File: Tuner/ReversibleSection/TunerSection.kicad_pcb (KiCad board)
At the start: 2 copper layers, 100 x 100 mm, 97 parts, among them J1 Conn_01x03, J10 Conn_01x02, J11 Conn_01x05, J12 Conn_01x01, J13 Conn_01x01, J14 Conn_01x01, J15 Conn_01x01, J2 Conn_01x03, J3 Conn_01x03, J4 Conn_01x03, J5 Conn_01x03, J6 Conn_01x03, J7 Conn_01x03, J8 Conn_01x02, J9 Conn_01x02, P10 Conn_01x01, P11 Conn_01x01, P12 Conn_01x01, P2 Conn_01x01, P3 Conn_01x01, P4 Conn_01x01, P5 Conn_01x01, P6 Conn_01x01, P7 Conn_01x01, P8 Conn_01x01, P9 Conn_01x01, U1 MCP23008, U2 ULN2803A

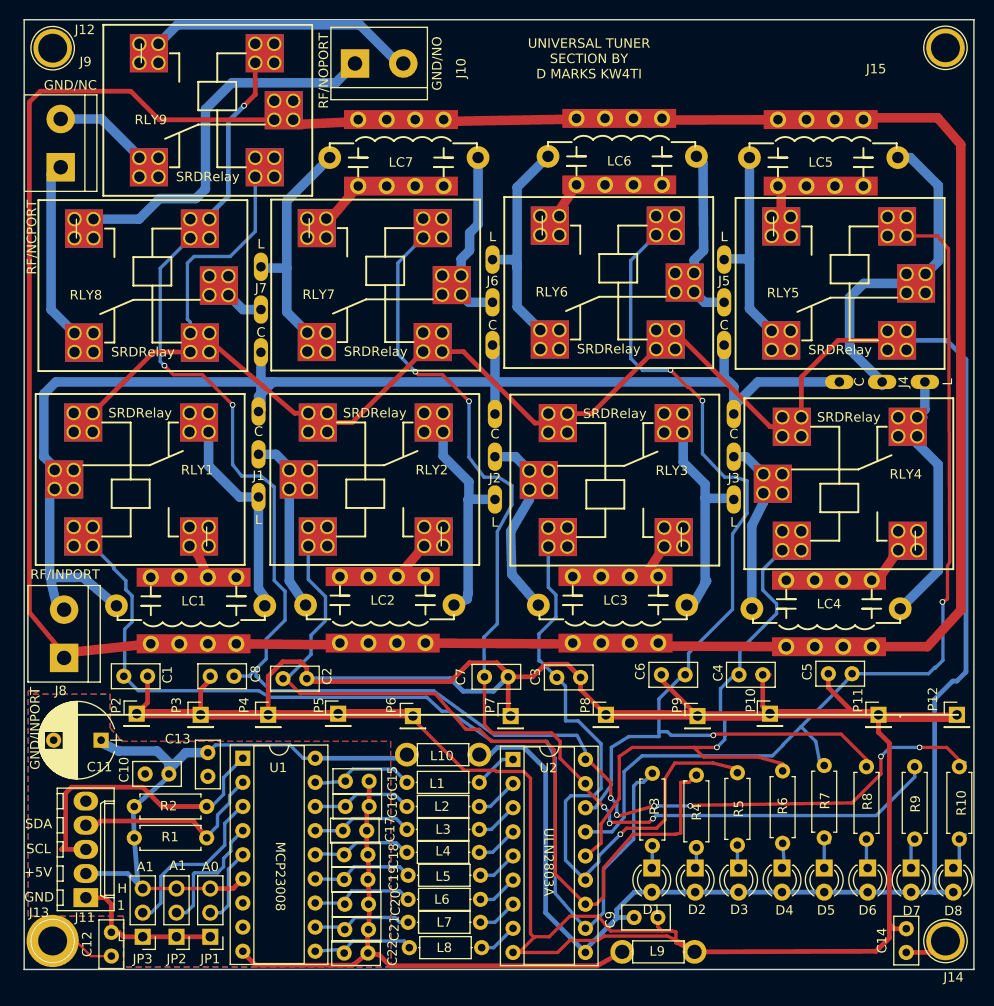
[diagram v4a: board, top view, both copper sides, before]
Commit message: JLCPCB submitted RelayControl version
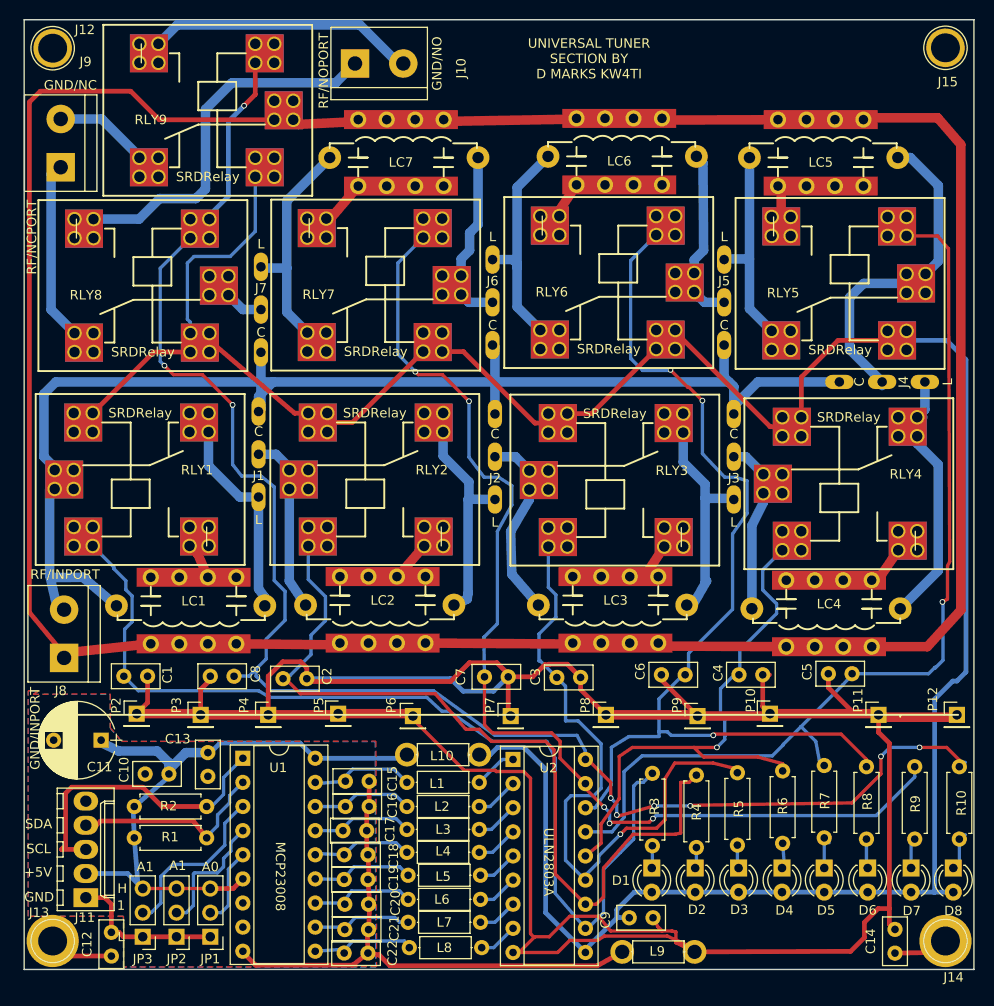
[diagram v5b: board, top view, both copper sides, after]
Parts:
- moved C14 1.19 mm to (141.7, 148.3)
- moved C9 0.51 mm to (113.7, 144.6)
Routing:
- net Net-(C14-Pad1): track 4.63 -> 5.82 mm
- net RLYPWR: track 264.9 -> 264.4 mm
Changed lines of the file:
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@@
     (thickness 1.6)
     (drawings 26)
-    (tracks 810)
+    (tracks 812)
     (zones 0)
     (modules 97)
@@
     (fp_circle (center 0 0) (end 2.6 0) (layer F.CrtYd) (width 0.05))
     (fp_circle (center 0 0) (end 0 -2.286) (layer F.SilkS) (width 0.12))
-    (pad 1 thru_hole circle (at 0 0) (size 4.064 4.064) (drill 3.048) (layers *.Cu *.Mask)
+    (pad 1 thru_hole circle (at 0 0) (size 5.5 5.5) (drill 3.048) (layers *.Cu *.Mask)
       (net 70 "Net-(C14-Pad1)"))
   )
@@
     (descr "module 1 pin (ou trou mecanique de percage)")
     (tags DEV)
-    (fp_text reference J15 (at -7.3 2.225) (layer F.SilkS)
+    (fp_text reference J15 (at 0.2413 3.59156) (layer F.SilkS)
       (effects (font (size 1 1) (thickness 0.15)))
     )
@@
     (descr "LED, diameter 3.0mm, 2 pins")
     (tags "LED diameter 3.0mm 2 pins")
-    (fp_text reference D1 (at 4.3815 0 360) (layer F.SilkS)
+    (fp_text reference D1 (at 1.31572 3.24104 360) (layer F.SilkS)
       (effects (font (size 1 1) (thickness 0.15)))
     )
@@
   )
   (module Capacitors_THT:C_Disc_D5.0mm_W2.5mm_P2.50mm (layer F.Cu)
-    (at 114.2238 144.526)
+    (at 113.71072 144.55648)
     (descr "C, Disc series, Radial, pin pitch=2.50mm, , diameter*width=5*2.5mm^2, Capacitor, http://cdn-reichelt.de/documents/datenblatt/B300/DS_KERKO_TC.pdf")
     (tags "C Disc series Radial pin pitch 2.50mm  diameter 5mm width 2.5mm Capacitor")
@@
   )
   (module Capacitors_THT:C_Disc_D5.0mm_W2.5mm_P2.50mm (layer F.Cu)
-    (at 142.875 148.209 90)
+    (at 141.68628 148.28012 90)
     (descr "C, Disc series, Radial, pin pitch=2.50mm, , diameter*width=5*2.5mm^2, Capacitor, http://cdn-reichelt.de/documents/datenblatt/B300/DS_KERKO_TC.pdf")
     (tags "C Disc series Radial pin pitch 2.50mm  diameter 5mm width 2.5mm Capacitor")
@@
   (segment (start 74.3326 57.8744) (end 74.3326 54.53836) (width 0.5) (layer F.Cu) (net 33) (status 20))
   (segment (start 67.5 72.994) (end 67.214 72.994) (width 0.35) (layer F.Cu) (net 33) (status 30))
+  (segment (start 69.342 127.167) (end 69.61696 127.167) (width 0.5) (layer B.Cu) (net 34) (status C00000))
+  (segment (start 69.61696 127.167) (end 70.63232 126.15164) (width 0.5) (layer B.Cu) (net 34) (status 400000))
+  (segment (start 79.03464 126.15164) (end 80.645 127.762) (width 0.5) (layer B.Cu) (net 34) (status 800000))
+  (segment (start 70.63232 126.15164) (end 79.03464 126.15164) (width 0.5) (layer B.Cu) (net 34))
   (segment (start 69.596 141.478) (end 72.009 141.478) (width 0.5) (layer F.Cu) (net 34))
   (segment (start 72.009 141.478) (end 73.025 140.462) (width 0.5) (layer F.Cu) (net 34))
@@
   (segment (start 80.645 127.762) (end 89.916 127.762) (width 0.5) (layer B.Cu) (net 34) (status 30))
   (segment (start 89.916 127.762) (end 90.297 127.381) (width 0.5) (layer B.Cu) (net 34) (status 30))
-  (segment (start 80.645 127.762) (end 79.375 127.762) (width 0.35) (layer B.Cu) (net 34) (status 10))
-  (segment (start 70.144 126.365) (end 69.342 127.167) (width 0.35) (layer B.Cu) (net 34) (status 20))
-  (segment (start 77.978 126.365) (end 70.144 126.365) (width 0.35) (layer B.Cu) (net 34))
-  (segment (start 79.375 127.762) (end 77.978 126.365) (width 0.35) (layer B.Cu) (net 34))
   (segment (start 61.722 136.017) (end 61.595 136.144) (width 0.35) (layer B.Cu) (net 34) (status 30))
   (segment (start 65.238 129.413) (end 65.238 128.945) (width 1) (layer B.Cu) (net 34) (status 30))
@@
   (segment (start 148.463 138.684) (end 147.828 139.319) (width 0.35) (layer B.Cu) (net 50))
   (segment (start 148.9456 135.9662) (end 149.098 135.8138) (width 0.35) (layer B.Cu) (net 50) (status 30))
-  (segment (start 142.875 145.709) (end 141.5815 145.709) (width 0.5) (layer F.Cu) (net 51))
+  (segment (start 141.097 143.5862) (end 139.92352 143.5862) (width 0.5) (layer F.Cu) (net 51))
+  (segment (start 138.47064 146.6342) (end 137.013916 148.090924) (width 0.5) (layer F.Cu) (net 51))
+  (segment (start 138.47064 145.03908) (end 138.47064 146.6342) (width 0.5) (layer F.Cu) (net 51))
+  (segment (start 139.92352 143.5862) (end 138.47064 145.03908) (width 0.5) (layer F.Cu) (net 51))
+  (segment (start 141.68628 145.78012) (end 141.5815 145.709) (width 0.5) (layer F.Cu) (net 51) (status 10))
   (segment (start 141.5815 145.709) (end 141.097 145.2245) (width 0.5) (layer F.Cu) (net 51))
-  (segment (start 116.7238 144.526) (end 116.7238 145.502) (width 0.35) (layer F.Cu) (net 51))
+  (segment (start 116.21072 144.55648) (end 116.7238 145.502) (width 0.35) (layer F.Cu) (net 51) (status 10))
   (segment (start 116.7238 145.502) (end 117.1702 145.9484) (width 0.35) (layer F.Cu) (net 51))
   (segment (start 90.932 123.317) (end 90.932 123.6345) (width 0.35) (layer F.Cu) (net 51))
@@
   (segment (start 99.568 129.032) (end 99.695 129.159) (width 0.35) (layer F.Cu) (net 51))
   (segment (start 96.3295 129.032) (end 99.568 129.032) (width 0.35) (layer F.Cu) (net 51))
-  (segment (start 120.5865 148.1455) (end 139.7 148.082) (width 0.5) (layer F.Cu) (net 51) (status 10))
+  (segment (start 120.5865 148.1455) (end 137.013916 148.090924) (width 0.5) (layer F.Cu) (net 51) (status 10))
   (segment (start 139.954 125.0315) (end 139.954 123.19) (width 0.5) (layer F.Cu) (net 51))
   (segment (start 141.097 126.1745) (end 139.954 125.0315) (width 0.5) (layer F.Cu) (net 51))
-  (segment (start 141.097 146.685) (end 141.097 145.2245) (width 0.5) (layer F.Cu) (net 51))
-  (segment (start 141.097 145.2245) (end 141.097 126.1745) (width 0.5) (layer F.Cu) (net 51))
-  (segment (start 139.7 148.082) (end 141.097 146.685) (width 0.5) (layer F.Cu) (net 51))
+  (segment (start 141.097 145.2245) (end 141.097 143.5862) (width 0.5) (layer F.Cu) (net 51))
+  (segment (start 141.097 143.5862) (end 141.097 126.1745) (width 0.5) (layer F.Cu) (net 51))
   (segment (start 62.992 119.126) (end 62.992 121.92) (width 0.5) (layer F.Cu) (net 51))
   (segment (start 62.992 121.92) (end 61.849 123.063) (width 0.5) (layer F.Cu) (net 51))
@@
   (segment (start 127.762 118.9736) (end 128.4732 118.9736) (width 0.5) (layer F.Cu) (net 51) (status 30))
   (segment (start 62.992 119.126) (end 62.992 119.3165) (width 0.5) (layer F.Cu) (net 51) (status 30))
-  (segment (start 114.2238 144.526) (end 112.4585 144.526) (width 0.5) (layer B.Cu) (net 52))
+  (segment (start 113.71072 144.55648) (end 112.4585 144.526) (width 0.5) (layer B.Cu) (net 52) (status 10))
   (segment (start 112.4585 144.526) (end 112.395 144.5895) (width 0.5) (layer B.Cu) (net 52))
   (segment (start 145.8595 141.859) (end 145.8595 121.539) (width 0.5) (layer B.Cu) (net 52))
@@
   (segment (start 98.171 147.701) (end 99.441 147.701) (width 0.35) (layer B.Cu) (net 68) (status 10))
   (segment (start 99.441 147.701) (end 101.473 145.669) (width 0.35) (layer B.Cu) (net 68) (status 20))
-  (segment (start 59.182 148.59) (end 57.023 148.59) (width 0.25) (layer F.Cu) (net 69))
-  (segment (start 55.433 147) (end 53 147) (width 0.25) (layer F.Cu) (net 69))
-  (segment (start 57.023 148.59) (end 55.433 147) (width 0.25) (layer F.Cu) (net 69))
-  (segment (start 142.875 148.209) (end 145.796 148.209) (width 0.5) (layer F.Cu) (net 70))
+  (segment (start 59.182 148.59) (end 54.59 148.59) (width 0.5) (layer F.Cu) (net 69))
+  (segment (start 54.59 148.59) (end 53 147) (width 0.5) (layer F.Cu) (net 69))
+  (segment (start 141.68628 148.28012) (end 145.796 148.209) (width 0.5) (layer F.Cu) (net 70) (status 10))
   (segment (start 145.796 148.209) (end 147.0025 147.0025) (width 0.5) (layer F.Cu) (net 70))
   (zone (net 25) (net_name GND) (layer F.Cu) (hatch edge 0.508)
@@
     (polygon
       (pts
-        (xy 50.927 121.031) (xy 59.055 120.9675) (xy 59.055 124.5235) (xy 60.2615 125.984) (xy 88.5825 125.984)
-        (xy 88.646 149.733) (xy 60.452 149.733) (xy 60.452 144.399) (xy 50.419 144.399) (xy 50.419 120.65)
+        (xy 50.927 121.031) (xy 59.055 120.9675) (xy 59.055 124.5235) (xy 60.2615 125.984) (xy 87.04326 125.9586)
+        (xy 87.10676 149.7076) (xy 60.452 149.733) (xy 60.452 144.399) (xy 50.419 144.399) (xy 50.419 120.65)
         (xy 50.673 120.65) (xy 51.562 120.65)
       )
@@
     (polygon
       (pts
-        (xy 50.927 121.031) (xy 59.055 121.031) (xy 59.055 124.587) (xy 60.2615 125.984) (xy 88.5825 125.984)
-        (xy 88.646 149.733) (xy 60.452 149.733) (xy 60.452 144.399) (xy 50.419 144.399) (xy 50.419 120.65)
+        (xy 50.927 121.031) (xy 59.055 121.031) (xy 59.055 124.587) (xy 60.2615 125.984) (xy 86.96198 126.0094)
+        (xy 87.02548 149.7584) (xy 60.452 149.733) (xy 60.452 144.399) (xy 50.419 144.399) (xy 50.419 120.65)
         (xy 50.673 120.65) (xy 51.562 120.65)
       )

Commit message: JLCPCB order 09232018 - improved grounding - improved I2C cabling - NEO7M port - support for common mode chokes - relay board now has capacitors on all coils
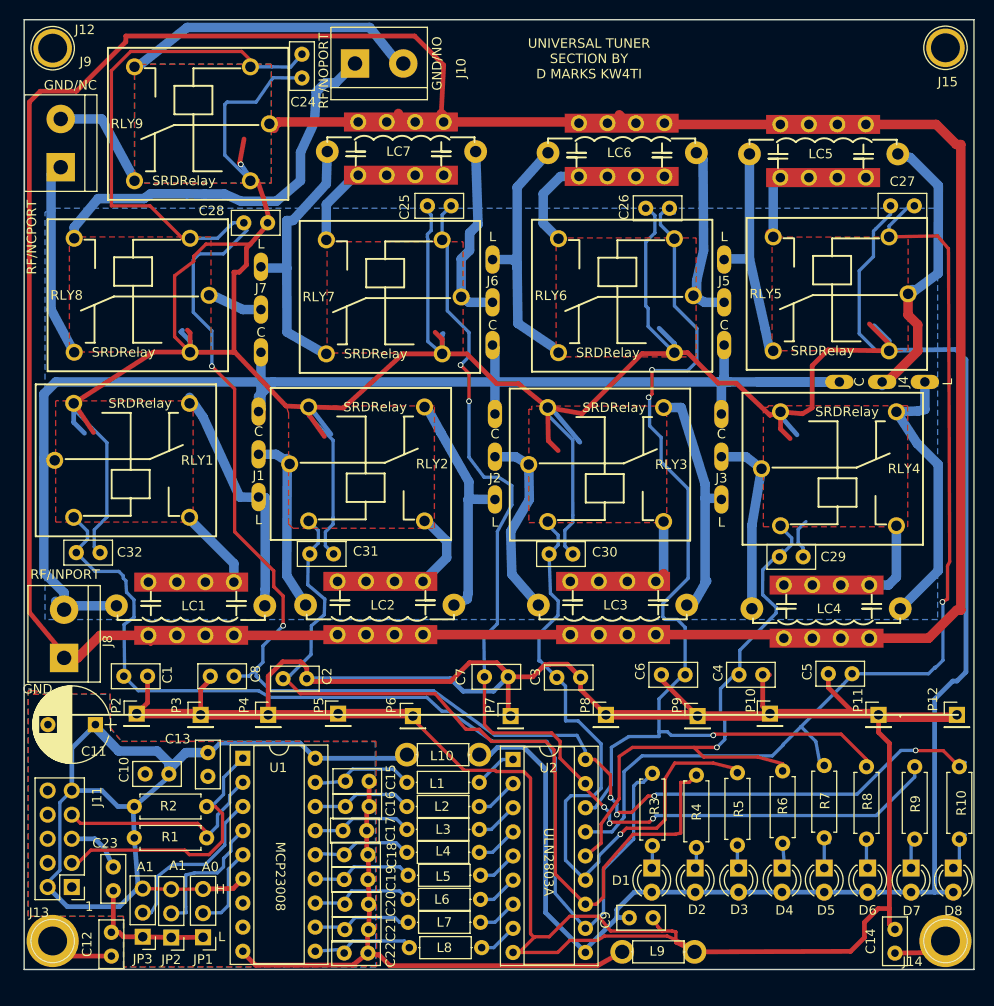
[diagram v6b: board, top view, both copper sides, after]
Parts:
- added C23: 100 nF, Capacitors_THT:C_Disc_D5.0mm_W2.5mm_P2.50mm, F.Cu at (59.4, 141.7)
- added C24: 10 nF, Capacitors_THT:C_Disc_D5.0mm_W2.5mm_P2.50mm, F.Cu at (79.2, 56.1)
- added C25: 10 nF, Capacitors_THT:C_Disc_D5.0mm_W2.5mm_P2.50mm, F.Cu at (92.5, 69.6)
- added C26: 10 nF, Capacitors_THT:C_Disc_D5.0mm_W2.5mm_P2.50mm, F.Cu at (115.4, 69.8)
- added C27: 10 nF, Capacitors_THT:C_Disc_D5.0mm_W2.5mm_P2.50mm, F.Cu at (141.2, 69.6)
- added C28: 10 nF, Capacitors_THT:C_Disc_D5.0mm_W2.5mm_P2.50mm, F.Cu at (75.6, 71.4)
- added C29: 10 nF, Capacitors_THT:C_Disc_D5.0mm_W2.5mm_P2.50mm, F.Cu at (132.0, 106.6)
- added C30: 10 nF, Capacitors_THT:C_Disc_D5.0mm_W2.5mm_P2.50mm, F.Cu at (107.8, 106.3)
- added C31: 10 nF, Capacitors_THT:C_Disc_D5.0mm_W2.5mm_P2.50mm, F.Cu at (82.6, 106.2)
- added C32: 10 nF, Capacitors_THT:C_Disc_D5.0mm_W2.5mm_P2.50mm, F.Cu at (58.0, 106.1)
- J11: value Conn_01x05 -> Conn_02x05_Odd_Even; footprint Connectors_Molex:Molex_KK-6410-05_05x2.54mm_Straight -> Pin_Headers:Pin_Header_Straight_2x05_Pitch2.54mm
- moved RLY9 2.55 mm to (67.8, 61.0)
- moved RLY8 2.03 mm to (61.5, 79.0)
- moved J11 1.86 mm to (55.0, 141.3), turned to 180 degrees
- moved RLY5 1.84 mm to (135.1, 78.9)
- moved C11 1.74 mm to (57.5, 124.2)
- moved J3 1.31 mm to (123.4, 96.0)
- moved RLY1 1.02 mm to (61.2, 96.4)
- moved JP1 0.76 mm to (68.8, 146.6)
- moved LC7 0.68 mm to (89.9, 63.9)
- moved RLY3 0.64 mm to (111.1, 96.8)
- moved RLY2 0.64 mm to (86.0, 96.8)
- moved RLY4 0.60 mm to (135.6, 97.3)
- moved JP2 0.56 mm to (65.5, 146.6)
- moved RLY6 0.39 mm to (112.5, 79.1)
- moved LC5 0.38 mm to (134.4, 64.1)
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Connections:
- net Net-(J11-Pad3) renamed SCL
- J11 pad 4: Net-(J11-Pad4) -> GND
- J11 pad 5: (no net) -> Net-(C23-Pad2)
- R1 pad 2: Net-(J11-Pad4) -> SDA
- U1 pad 2: Net-(J11-Pad4) -> SDA
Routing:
- net RLYPWR: track 264.4 -> 468.2 mm, vias 0 -> 1
- net RLY8: track 166.0 -> 200.9 mm, vias 9 -> 6
- net +5V: track 69.3 -> 102.3 mm
- net SDA: track 0.00 -> 23.0 mm
- net Net-(J11-Pad4): track 21.2 -> 0.00 mm
- net RFGND: track 264.9 -> 281.2 mm
- net RFPORT1: track 144.4 -> 153.6 mm
- net RLY1: track 103.5 -> 110.8 mm
- net RLY5: track 101.9 -> 108.4 mm
- net Net-(LC6-Pad1): track 3.84 -> 9.92 mm
- net Net-(C23-Pad2): track 0.00 -> 6.03 mm
- net Net-(LC1-Pad1): track 3.88 -> 8.76 mm
- net Net-(J7-Pad1): track 24.2 -> 29.1 mm
- net Net-(J4-Pad1): track 25.4 -> 29.9 mm
- net RLY4: track 58.4 -> 62.8 mm
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- added copper zone on B.Cu, net RLYPWR
- added copper zone on F.Cu, net RLYPWR
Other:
- board text removed: "+5V"
- board text removed: "GND/INPORT"
- board text removed: "SCL"
- board text removed: "SDA"

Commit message: Relay boards changed to have coil terminals all on same side
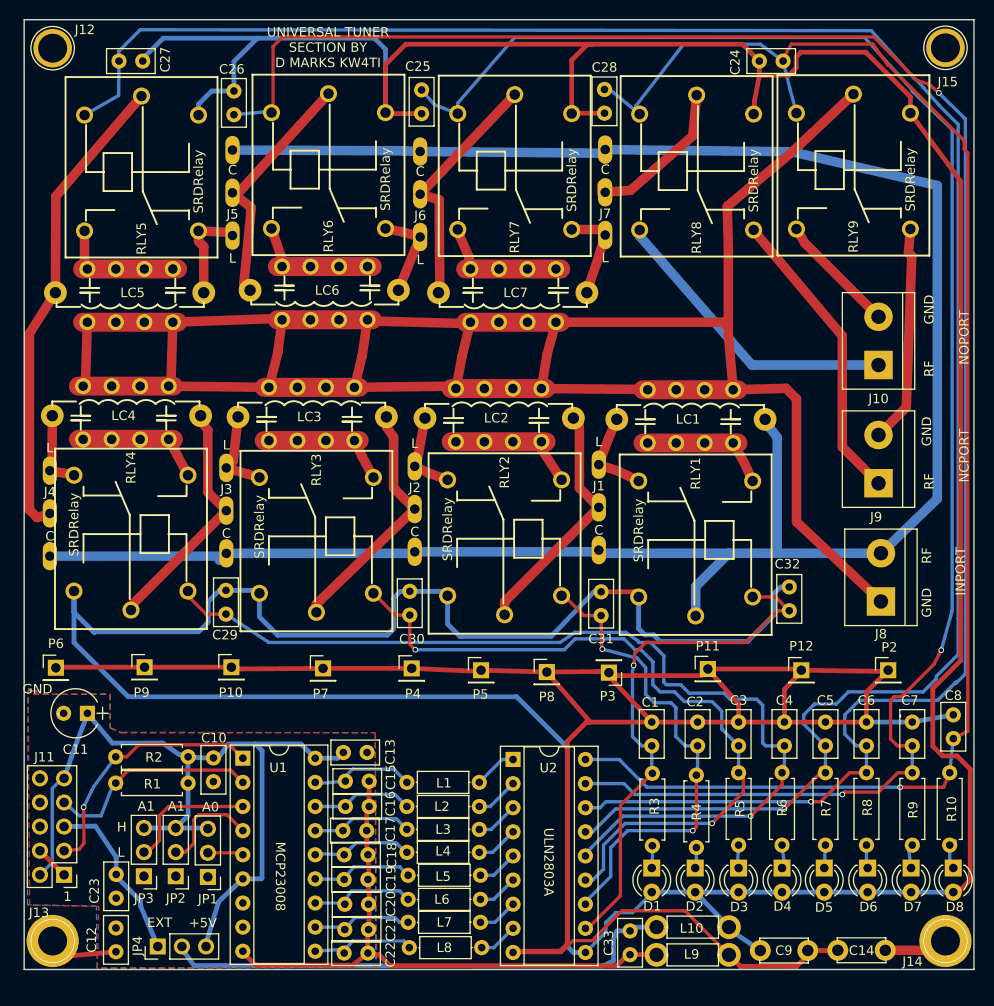
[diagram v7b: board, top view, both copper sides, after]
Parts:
- added C33: 100 nF, Capacitors_THT:C_Disc_D5.0mm_W2.5mm_P2.50mm, F.Cu at (113.8, 148.4)
- added JP4: Jumper_NC_Dual, Pin_Headers:Pin_Header_Straight_1x03_Pitch2.54mm, F.Cu at (64.1, 147.6)
- C11: footprint Capacitors_THT:CP_Radial_D8.0mm_P5.00mm -> Capacitors_THT:CP_Radial_Tantal_D5.0mm_P2.50mm
- C14, C9: footprint Capacitors_THT:C_Disc_D5.0mm_W2.5mm_P2.50mm -> Capacitors_THT:C_Disc_D5.0mm_W2.5mm_P5.00mm
- moved J9 92.3 mm to (140.0, 98.8)
- moved J4 88.7 mm to (52.7, 102.0), turned to 270 degrees
- moved J8 86.2 mm to (140.2, 111.3)
- moved C27 80.2 mm to (62.5, 54.4), turned to 180 degrees
- moved P2 79.3 mm to (141.0, 118.5)
- moved C8 78.3 mm to (147.8, 123.2), turned to 270 degrees
- moved LC4 76.0 mm to (61.0, 91.7), turned to 90 degrees
- moved LC5 74.9 mm to (60.9, 78.7), turned to 270 degrees
- moved RLY4 74.7 mm to (61.2, 104.2), turned to 90 degrees
- moved RLY5 73.8 mm to (62.4, 66.0), turned to 270 degrees
- moved C32 72.7 mm to (130.6, 109.7), turned to 270 degrees
- moved RLY9 69.7 mm to (137.3, 65.8), turned to 270 degrees
- moved J10 63.6 mm to (140.0, 86.4), turned to 90 degrees
- moved C29 60.9 mm to (71.2, 110.1), turned to 270 degrees
- moved RLY8 60.8 mm to (120.8, 65.9), turned to 270 degrees
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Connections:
- L10 pad 1: +5V -> EXTPWR
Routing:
- net RLY5: track 108.4 -> 212.9 mm
- net RLY6: track 106.5 -> 199.9 mm, vias 3 -> 2
- net RFGND: track 281.2 -> 194.3 mm
- net RFPORT1: track 153.6 -> 228.5 mm
- net RLYGND: track 294.8 -> 234.6 mm
- net RLY7: track 116.2 -> 174.1 mm, vias 5 -> 2
- net EXTPWR: track 0.00 -> 54.7 mm
- net RLY1: track 110.8 -> 56.1 mm, vias 0 -> 1
- net RLY2: track 92.4 -> 51.7 mm, vias 0 -> 2
- net RLY4: track 62.8 -> 103.2 mm
- net RLY8: track 200.9 -> 164.5 mm, vias 6 -> 1
- net Net-(J4-Pad1): track 29.9 -> 8.48 mm
- net Net-(J4-Pad2): track 30.8 -> 50.3 mm
- net Net-(J6-Pad1): track 28.6 -> 9.82 mm
- net Net-(J10-Pad2): track 31.3 -> 12.7 mm
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- removed copper zone on B.Cu, net RLYPWR
- removed copper zone on F.Cu, net RLYPWR
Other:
- board text added: "+5V"
- board text added: "EXT"
- board text added: "INPORT"
- board text added: "NCPORT"
- board text added: "NOPORT"
- board text added: "RF"
- board text removed: "GND/NC"
- board text removed: "GND/NO"
- board text removed: "RF/INPORT"
- board text removed: "RF/NCPORT"
- board text removed: "RF/NOPORT"
